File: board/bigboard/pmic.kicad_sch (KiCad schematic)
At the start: 22 parts, among them U2 MAX20353AEWN+

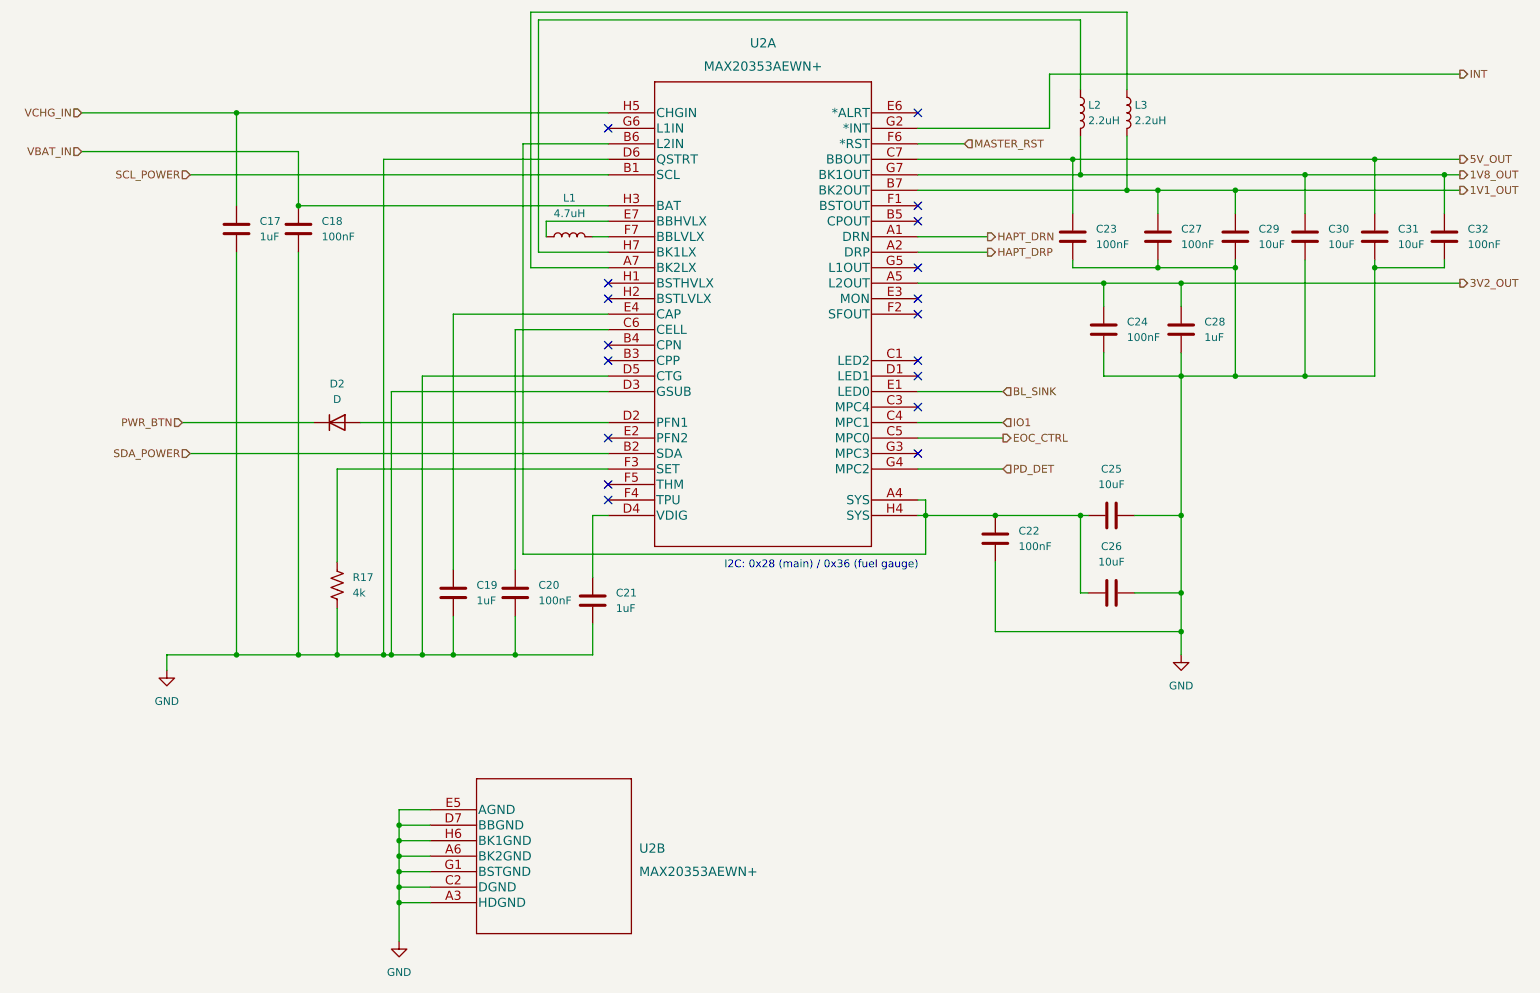
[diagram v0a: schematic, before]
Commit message: Manufactured version of bigboard
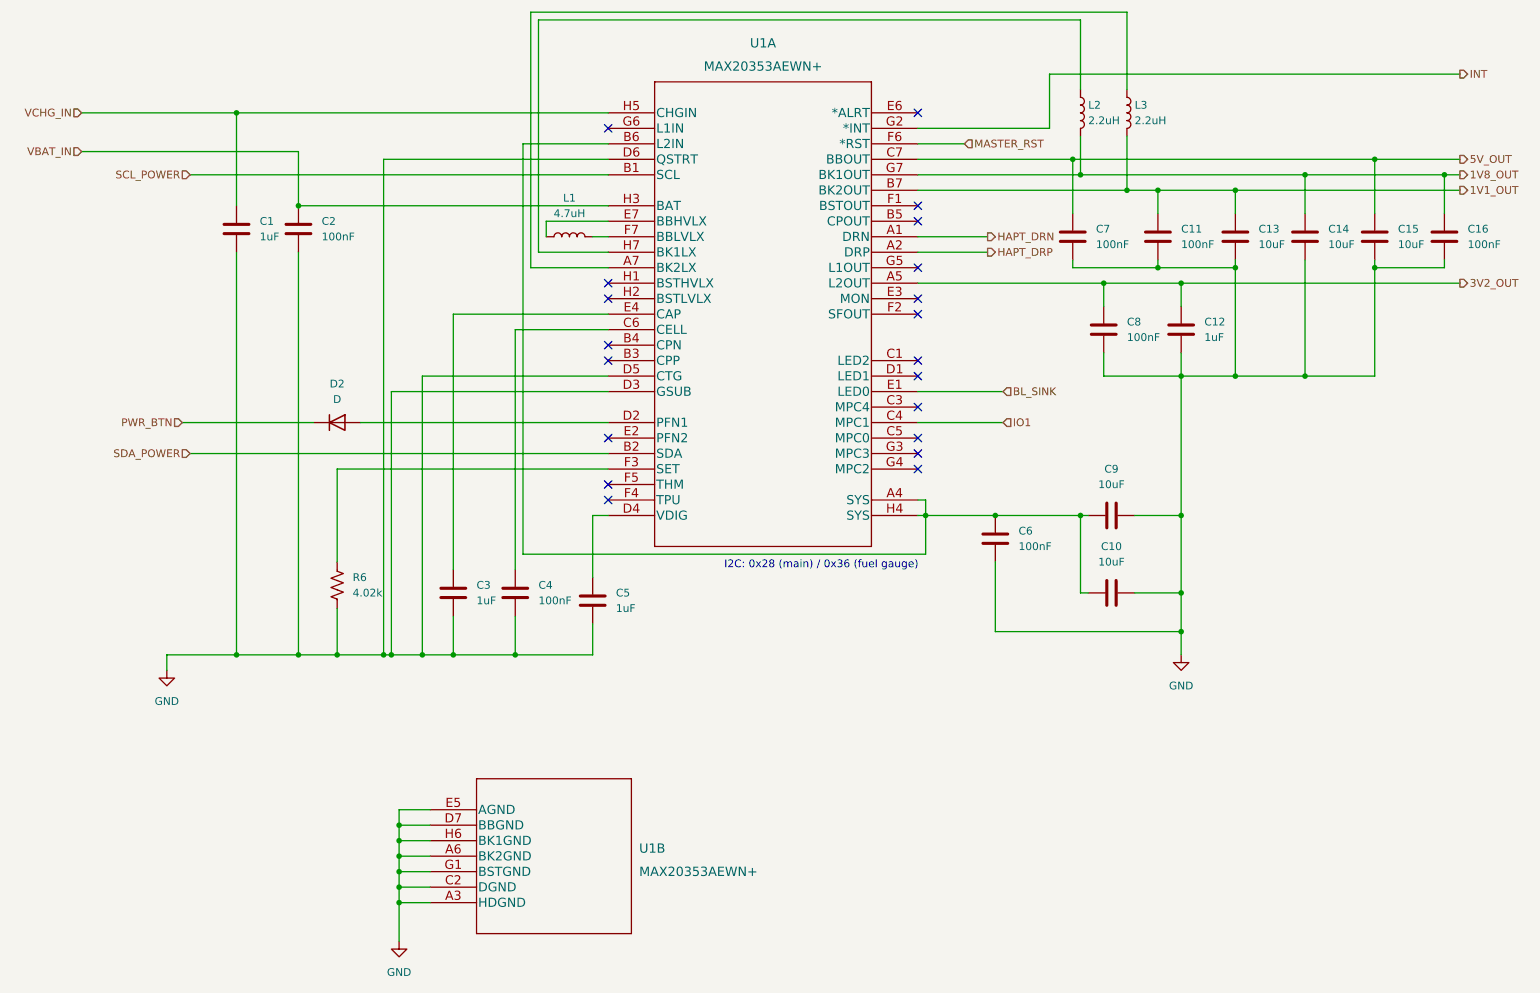
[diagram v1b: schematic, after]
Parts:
- C1: renamed from C17; footprint Capacitor_SMD:C_0201_0603Metric -> Capacitor_SMD:C_0603_1608Metric; MPN (none) -> CC0603KRX5R7BB105
- C10: renamed from C26; MPN (none) -> GRM188R61E106KA73D
- C11: renamed from C27; MPN (none) -> CC0201KRX5R8BB104
- C12: renamed from C28; MPN (none) -> CC0201MRX5R6BB105
- C13: renamed from C29; MPN (none) -> GRM188R61E106KA73D
- C14: renamed from C30; MPN (none) -> GRM188R61E106KA73D
- C15: renamed from C31; MPN (none) -> GRM188R61E106KA73D
- C16: renamed from C32; MPN (none) -> CC0201KRX5R8BB104
- C2: renamed from C18; MPN (none) -> CC0201KRX5R8BB104
- C3: renamed from C19; MPN (none) -> CC0201MRX5R6BB105
- C4: renamed from C20; MPN (none) -> CC0201KRX5R8BB104
- C5: renamed from C21; MPN (none) -> CC0201MRX5R6BB105
- C6: renamed from C22; MPN (none) -> CC0201KRX5R8BB104
- C7: renamed from C23; MPN (none) -> CC0201KRX5R8BB104
- C8: renamed from C24; MPN (none) -> CC0201KRX5R8BB104
- C9: renamed from C25; MPN (none) -> GRM188R61E106KA73D
- L1: MPN (none) -> MLP2012V4R7MT0S1
- L2, L3: MPN (none) -> DFE201210U-2R2M=P2
- R6: renamed from R17; value 4k -> 4.02k; MPN (none) -> RC0201FR-074K02L
- renumbered U2 to U1
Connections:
- net EOC_CTRL: no longer names the net of U1.C5 (MPC0)
- net PD_DET: no longer names the net of U1.G4 (MPC2)
- no-connect marks 18 -> 20

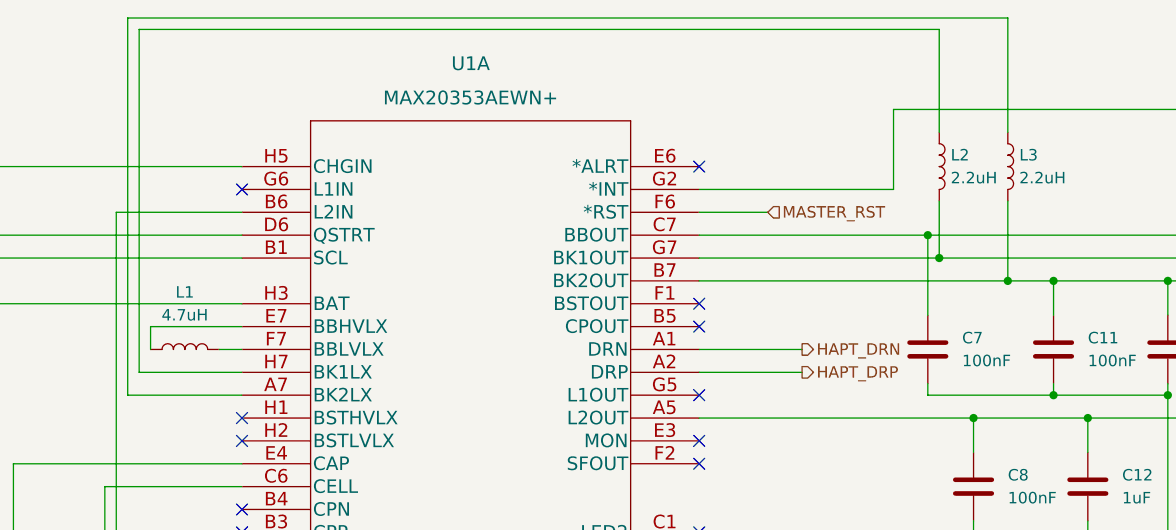
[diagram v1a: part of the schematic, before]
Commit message: Update board to kicad 7
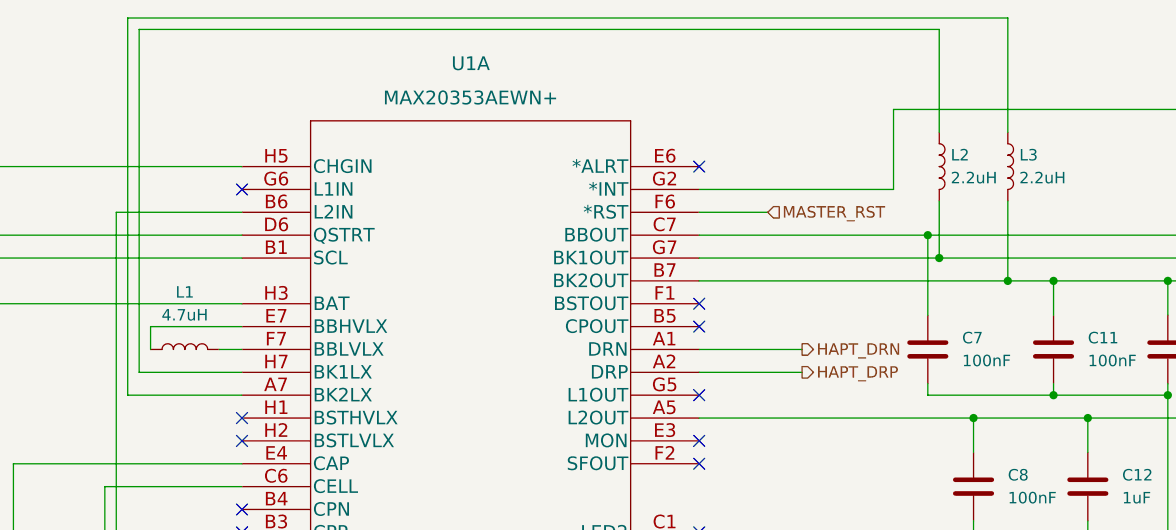
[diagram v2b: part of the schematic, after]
